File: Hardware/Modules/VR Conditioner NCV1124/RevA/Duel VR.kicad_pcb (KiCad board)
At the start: 2 copper layers, 22.9 x 20.1 mm, 15 parts, among them IC1 NCV1124, J1 Speedy VR Mount

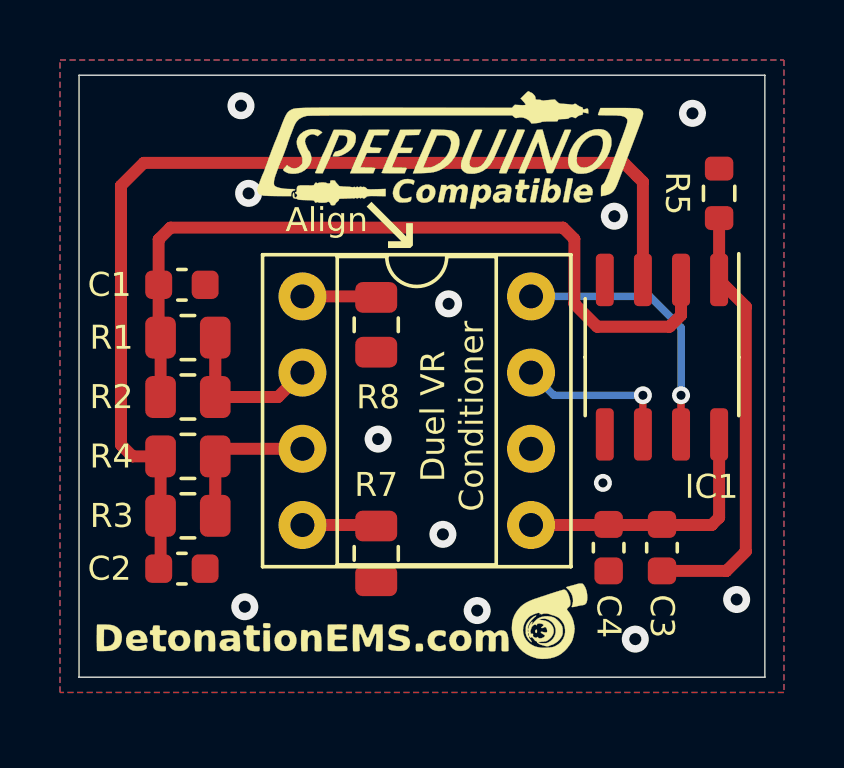
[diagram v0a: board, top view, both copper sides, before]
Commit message: Schematic Correction
VRConditioner NCV1124 schematic math correction.
Readme Updated for upcoming revision
Instructions Added to RevA folder
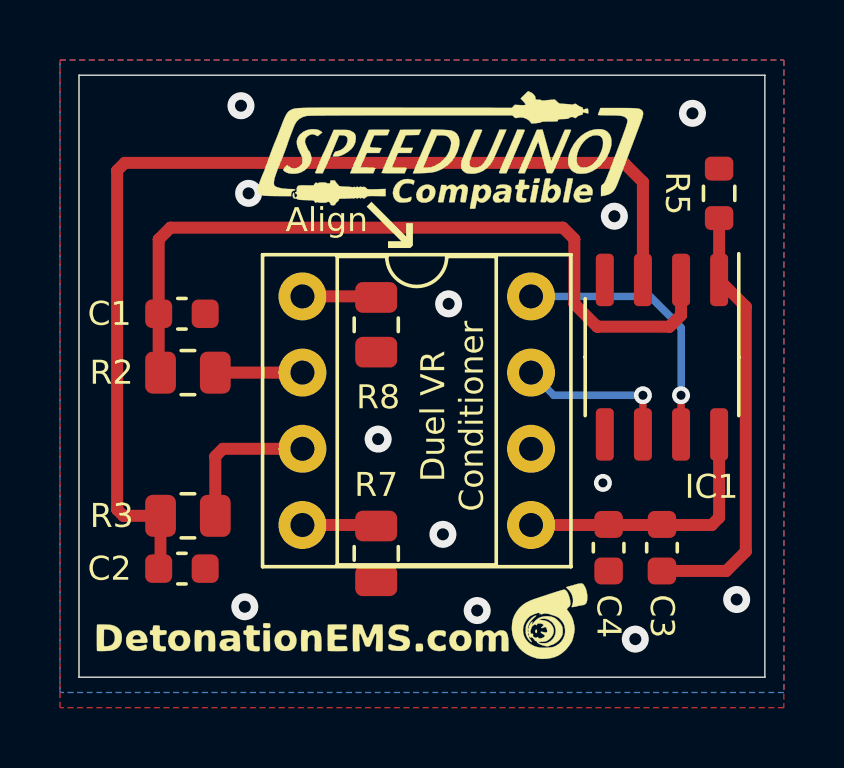
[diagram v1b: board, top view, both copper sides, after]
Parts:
- removed R1, R4: 16k, Resistor_SMD:R_0805_2012Metric
- moved C1 0.97 mm to (157.5, 90.8)
- moved R2 0.81 mm to (157.7, 92.7)
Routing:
- net VR1+: track 5.22 -> 2.91 mm
- net Net-(C1-Pad2): track 26.8 -> 26.0 mm
- net Net-(C2-Pad1): track 35.1 -> 35.8 mm
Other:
- board text removed: "JP1 - CRANK JP2 - CAM"
